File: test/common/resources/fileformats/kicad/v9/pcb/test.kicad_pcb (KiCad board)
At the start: 2 copper layers, 4 parts

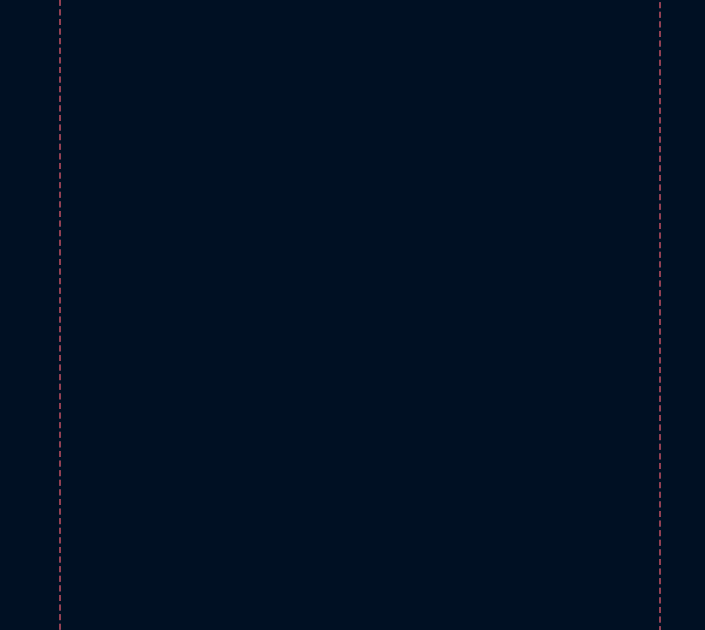
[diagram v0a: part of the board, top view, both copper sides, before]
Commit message: KiCad: Fix S-expression string escape handling (#1789)
## Description

Fix `_unescape_string` and `writeEscapedString` in the Zig S-expression
engine to properly handle backslash escape sequences (`\\n`, `\\r`,
`\\\\`, `\\"`).

Previously, `_unescape_string` stripped all backslashes
indiscriminately, turning `\\n` into `n`. And `writeEscapedString` only
escaped double quotes, not newlines or backslashes. This caused data
corruption on round-trip: e.g. multi-line silkscreen text in a KiCad
layout would collapse onto a single line after a build.

## Motivation

Running an atopile build on a `.kicad_pcb` that contained `\\n` in a
quoted string (e.g. multi-line silkscreen text) would replace the
newline with the literal character `n`, corrupting the layout.

---------

Co-authored-by: ruben-iteng <94007802+ruben-iteng@users.noreply.github.com>
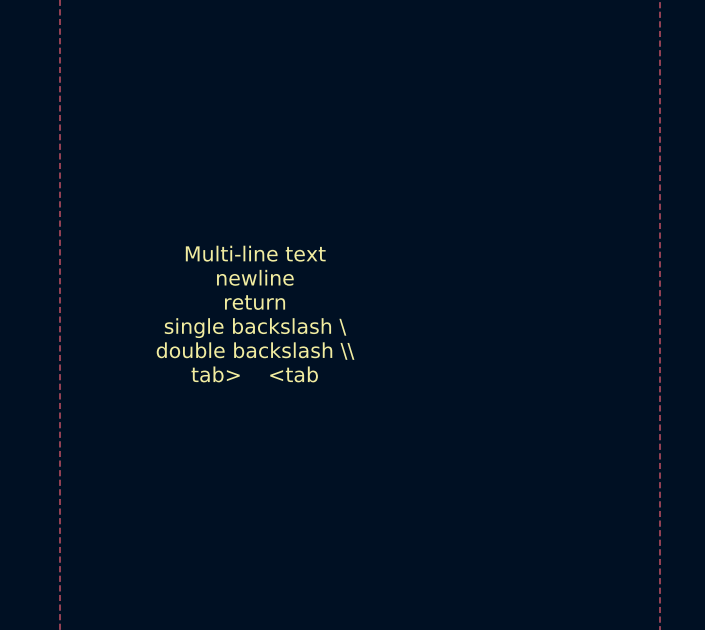
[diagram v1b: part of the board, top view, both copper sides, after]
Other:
- board text added: "Multi-line text newline returnr single backslash \ double backslash \\ tab> <tab"
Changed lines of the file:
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@@
+		)
+	)
+	(gr_text "Multi-line text\nnewline\nreturn\r\nsingle backslash \\\ndouble backslash \\\\\ntab>	<tab"
+		(at 26.5 31.5 0)
+		(layer "F.SilkS")
+		(effects
+			(font
+				(size 0.5 0.5)
+				(thickness 0.1)
+			)
 		)
 	)
